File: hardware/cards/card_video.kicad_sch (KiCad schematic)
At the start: 30 parts, among them J1 HDMI_A, J2 VGA HD15, M1 Core2350B (8MB PSRAM), U2 74LVC245A, U3 74LVC245A, U4 74LVC245A, U5 74LVC245A, U6 74LVC245A, U7 74LVC245A

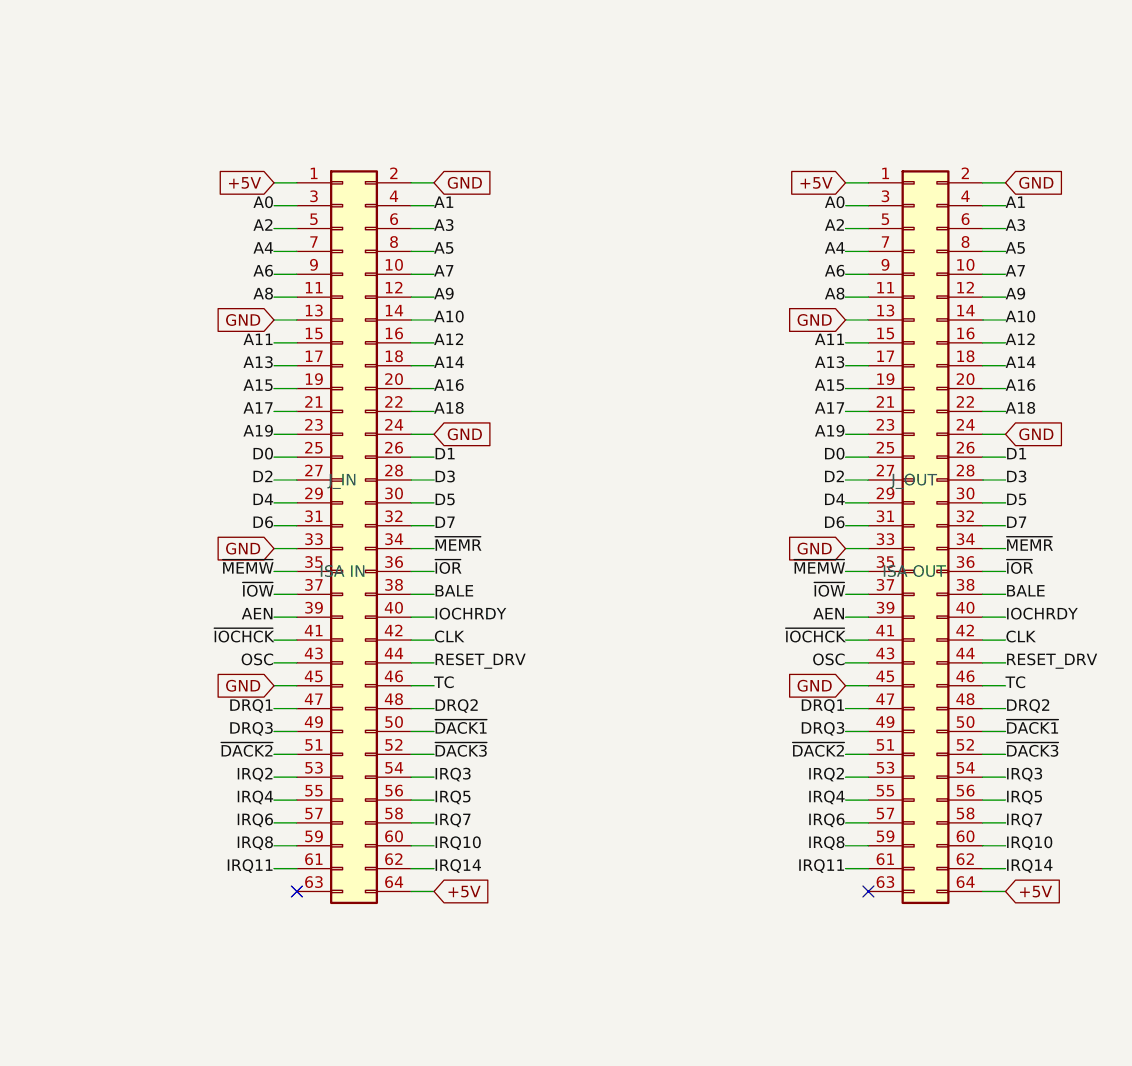
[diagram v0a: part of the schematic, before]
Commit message: Re-base ISA connector on standard 8-bit ISA pinout (60-pin, PicoGUS-style)
isa_conn now uses the standard 8-bit ISA edge pinout on a 60-pin 2.54mm header
(Conn_02x30_Odd_Even), matching the PicoGUS Bus_ISA_8bit layout so the sidecar and
dev cards are pin-compatible with real ISA cards (and 60-pin ribbon is easy to
source). The unused ISA analog rails are reclaimed: pin7 -5V->~{IOCHCK}, pin11
-12V->GND (extra return), pin15 +12V->IRQ8; pin13 reserved/0WS# left NC. Drops the
non-standard IRQ10/11/14 (16-bit-extension signals on a real AT); DACK0/REFRESH#
now on its standard pin (undriven, for card compatibility). Change is confined to
isa_conn.py; sidecar + all card_* sheets inherit it. Verified pin map and
connectivity (IOCHCK->Bus MCU, IRQ8->collector+RTC); zero structural ERC on
motherboard and all five cards.

Co-Authored-By: Claude Opus 4.8 (1M context) <noreply@anthropic.com>
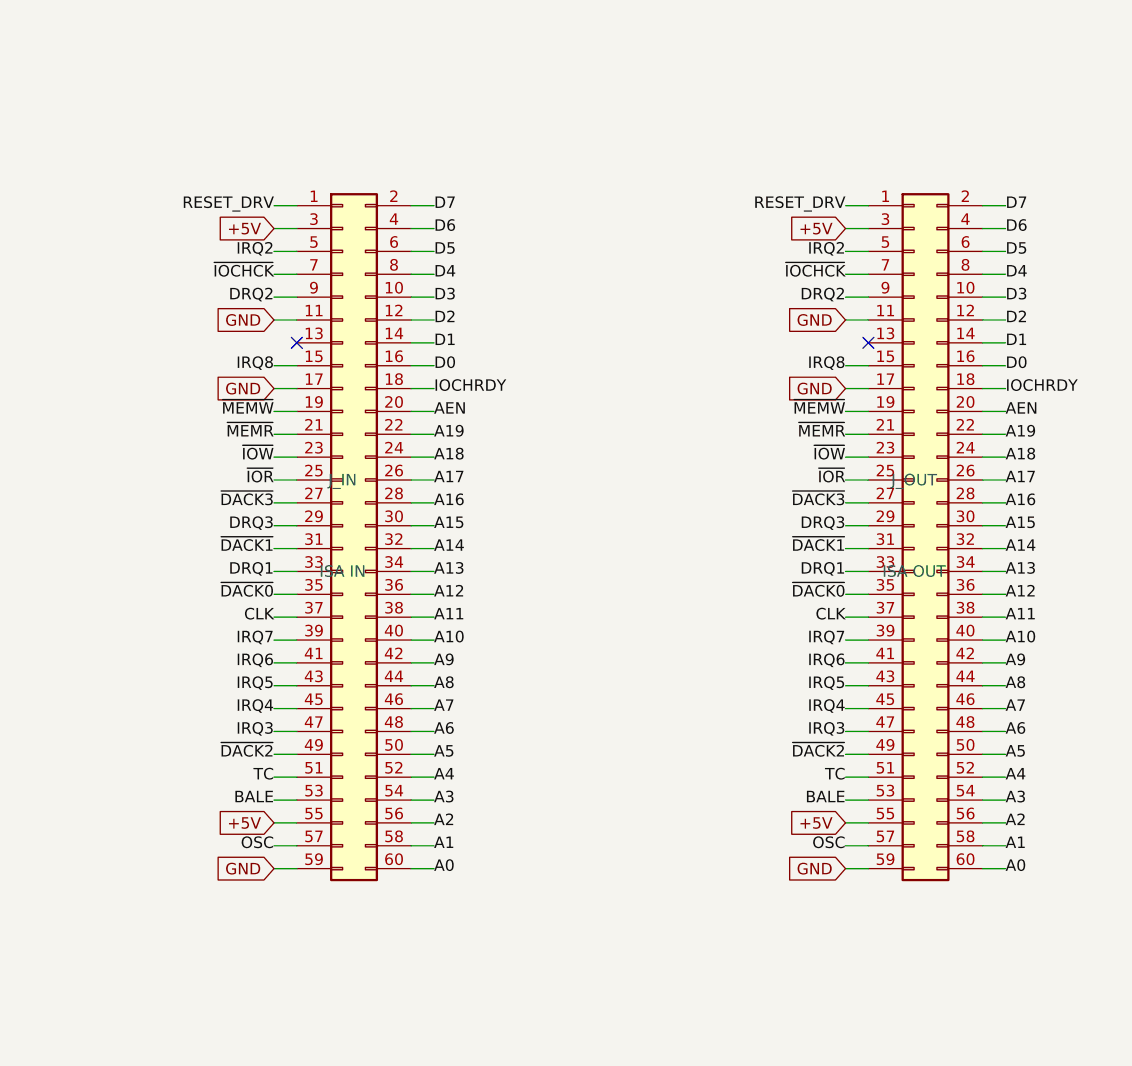
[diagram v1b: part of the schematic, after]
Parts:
- removed J_IN: ISA IN, symbol Connector_Generic:Conn_02x32_Odd_Even
- removed J_OUT: ISA OUT, symbol Connector_Generic:Conn_02x32_Odd_Even
- added J_IN: ISA IN, symbol Connector_Generic:Conn_02x30_Odd_Even
- added J_OUT: ISA OUT, symbol Connector_Generic:Conn_02x30_Odd_Even
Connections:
- net +5V: now also J_IN.3 (Pin_3), J_IN.55 (Pin_55), J_OUT.3 (Pin_3), J_OUT.55 (Pin_55)
- net A0: now also J_IN.60 (Pin_60), J_OUT.60 (Pin_60)
- net A1: now also J_IN.58 (Pin_58), J_OUT.58 (Pin_58)
- net A10: now also J_IN.40 (Pin_40), J_OUT.40 (Pin_40)
- net A11: now also J_IN.38 (Pin_38), J_OUT.38 (Pin_38)
- net A12: now also J_IN.36 (Pin_36), J_OUT.36 (Pin_36)
- net A13: now also J_IN.34 (Pin_34), J_OUT.34 (Pin_34)
- net A14: now also J_IN.32 (Pin_32), J_OUT.32 (Pin_32)
- net A15: now also J_IN.30 (Pin_30), J_OUT.30 (Pin_30)
- net A16: now also J_IN.28 (Pin_28), J_OUT.28 (Pin_28)
- net A17: now also J_IN.26 (Pin_26), J_OUT.26 (Pin_26)
- net A18: now also J_IN.24 (Pin_24), J_OUT.24 (Pin_24)
- net A19: now also J_IN.22 (Pin_22), J_OUT.22 (Pin_22)
- net A2: now also J_IN.56 (Pin_56), J_OUT.56 (Pin_56)
- net A3: now also J_IN.54 (Pin_54), J_OUT.54 (Pin_54)
- net A4: now also J_IN.52 (Pin_52), J_OUT.52 (Pin_52)
- net A5: now also J_IN.50 (Pin_50), J_OUT.50 (Pin_50)
- net A6: now also J_IN.48 (Pin_48), J_OUT.48 (Pin_48)
- net A7: now also J_IN.46 (Pin_46), J_OUT.46 (Pin_46)
- net A8: now also J_IN.44 (Pin_44), J_OUT.44 (Pin_44)
- net A9: now also J_IN.42 (Pin_42), J_OUT.42 (Pin_42)
- net AEN: now also J_IN.20 (Pin_20), J_OUT.20 (Pin_20)
- net BALE: now also J_IN.53 (Pin_53), J_OUT.53 (Pin_53)
- net CLK: now also J_IN.37 (Pin_37), J_OUT.37 (Pin_37)
- net D0: now also J_IN.16 (Pin_16), J_OUT.16 (Pin_16)
- net D1: now also J_IN.14 (Pin_14), J_OUT.14 (Pin_14)
- net D2: now also J_IN.12 (Pin_12), J_OUT.12 (Pin_12)
- net D3: now also J_IN.10 (Pin_10), J_OUT.10 (Pin_10)
- net D4: now also J_IN.8 (Pin_8), J_OUT.8 (Pin_8)
- net D5: now also J_IN.6 (Pin_6), J_OUT.6 (Pin_6)
- net D6: now also J_IN.4 (Pin_4), J_OUT.4 (Pin_4)
- net D7: now also J_IN.2 (Pin_2), J_OUT.2 (Pin_2)
- net DRQ1: now also J_IN.33 (Pin_33), J_OUT.33 (Pin_33)
- net DRQ2: now also J_IN.9 (Pin_9), J_OUT.9 (Pin_9)
- net DRQ3: now also J_IN.29 (Pin_29), J_OUT.29 (Pin_29)
- net GND: now also J_IN.11 (Pin_11), J_IN.17 (Pin_17), J_IN.59 (Pin_59), J_OUT.11 (Pin_11), J_OUT.17 (Pin_17), J_OUT.59 (Pin_59)
- net IOCHRDY: now also J_IN.18 (Pin_18), J_OUT.18 (Pin_18)
- net IRQ2: now also J_IN.5 (Pin_5), J_OUT.5 (Pin_5)
- net IRQ3: now also J_IN.47 (Pin_47), J_OUT.47 (Pin_47)
- net IRQ4: now also J_IN.45 (Pin_45), J_OUT.45 (Pin_45)
- net IRQ5: now also J_IN.43 (Pin_43), J_OUT.43 (Pin_43)
- net IRQ6: now also J_IN.41 (Pin_41), J_OUT.41 (Pin_41)
- net IRQ7: now also J_IN.39 (Pin_39), J_OUT.39 (Pin_39)
- net IRQ8: now also J_IN.15 (Pin_15), J_OUT.15 (Pin_15)
- net OSC: now also J_IN.57 (Pin_57), J_OUT.57 (Pin_57)
- net RESET_DRV: now also J_IN.1 (Pin_1), J_OUT.1 (Pin_1)
- net TC: now also J_IN.51 (Pin_51), J_OUT.51 (Pin_51)
- net ~{DACK1}: now also J_IN.31 (Pin_31), J_OUT.31 (Pin_31)
- net ~{DACK2}: now also J_IN.49 (Pin_49), J_OUT.49 (Pin_49)
- net ~{DACK3}: now also J_IN.27 (Pin_27), J_OUT.27 (Pin_27)
- net ~{IOCHCK}: now also J_IN.7 (Pin_7), J_OUT.7 (Pin_7)
- net ~{IOR}: now also J_IN.25 (Pin_25), J_OUT.25 (Pin_25)
- net ~{IOW}: now also J_IN.23 (Pin_23), J_OUT.23 (Pin_23)
- net ~{MEMR}: now also J_IN.21 (Pin_21), J_OUT.21 (Pin_21)
- net ~{MEMW}: now also J_IN.19 (Pin_19), J_OUT.19 (Pin_19)
- new net ~{DACK0}: J_IN.35 (Pin_35), J_OUT.35 (Pin_35)

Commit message: Drive ISA REFRESH# from the Bus MCU for DRAM-based cards
Pin 35 (DACK0/REFRESH#) net renamed ~{DACK0} -> ~{REFRESH} in isa_conn and is now
an active Bus MCU output (GPIO47, reclaimed from the redundant raw-~WR sense -- the
MCU tracks writes via the gated MEMW/IOW). Driven from the internal ~15us refresh
timer (same source as the 0x61-bit-4 toggle); a refresh cycle reuses the bus-master
engine to walk the row address on A0-A7 + pulse MEMR#, so DRAM ISA cards see a
standard refresh. ~{REFRESH} added to the Bus MCU interface. Verified it ties
sidecar<->Bus MCU and passes through J_IN<->J_OUT on every dev card; zero
structural ERC on motherboard and all five cards.

Co-Authored-By: Claude Opus 4.8 (1M context) <noreply@anthropic.com>
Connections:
- net ~{DACK0} renamed ~{REFRESH}
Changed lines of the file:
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@@
 		)
 	)
-	(label "~{DACK0}"
+	(label "~{REFRESH}"
 		(at 436.88 160.02 180)
 		(effects
@@
 		)
 	)
-	(label "~{DACK0}"
+	(label "~{REFRESH}"
 		(at 500.38 160.02 180)
 		(effects
@@
 		(instances
 			(project "card_video"
-				(path "/374d94a5-2c53-4835-9847-49239f55f3cf"
+				(path "/0c25f20b-85af-4bd6-a748-56afc32eeb49"
 					(reference "J_IN")
 					(unit 1)
@@
 		(instances
 			(project "card_video"
-				(path "/374d94a5-2c53-4835-9847-49239f55f3cf"
+				(path "/0c25f20b-85af-4bd6-a748-56afc32eeb49"
 					(reference "J_OUT")
 					(unit 1)
@@
 		(instances
 			(project "card_video"
-				(path "/374d94a5-2c53-4835-9847-49239f55f3cf"
+				(path "/0c25f20b-85af-4bd6-a748-56afc32eeb49"
 					(reference "M1")
 					(unit 1)
@@
 		(instances
 			(project "card_video"
-				(path "/374d94a5-2c53-4835-9847-49239f55f3cf"
+				(path "/0c25f20b-85af-4bd6-a748-56afc32eeb49"
 					(reference "C1")
 					(unit 1)
@@
 		(instances
 			(project "card_video"
-				(path "/374d94a5-2c53-4835-9847-49239f55f3cf"
+				(path "/0c25f20b-85af-4bd6-a748-56afc32eeb49"
 					(reference "C2")
 					(unit 1)
@@
 		(instances
 			(project "card_video"
-				(path "/374d94a5-2c53-4835-9847-49239f55f3cf"
+				(path "/0c25f20b-85af-4bd6-a748-56afc32eeb49"
 					(reference "C3")
 					(unit 1)
@@
 		(instances
 			(project "card_video"
-				(path "/374d94a5-2c53-4835-9847-49239f55f3cf"
+				(path "/0c25f20b-85af-4bd6-a748-56afc32eeb49"
 					(reference "U2")
 					(unit 1)
@@
 		(instances
 			(project "card_video"
-				(path "/374d94a5-2c53-4835-9847-49239f55f3cf"
+				(path "/0c25f20b-85af-4bd6-a748-56afc32eeb49"
 					(reference "U3")
 					(unit 1)
@@
 		(instances
 			(project "card_video"
-				(path "/374d94a5-2c53-4835-9847-49239f55f3cf"
+				(path "/0c25f20b-85af-4bd6-a748-56afc32eeb49"
 					(reference "U4")
 					(unit 1)
@@
 		(instances
 			(project "card_video"
-				(path "/374d94a5-2c53-4835-9847-49239f55f3cf"
+				(path "/0c25f20b-85af-4bd6-a748-56afc32eeb49"
 					(reference "U5")
 					(unit 1)
@@
 		(instances
 			(project "card_video"
-				(path "/374d94a5-2c53-4835-9847-49239f55f3cf"
+				(path "/0c25f20b-85af-4bd6-a748-56afc32eeb49"
 					(reference "U6")
 					(unit 1)
@@
 		(instances
 			(project "card_video"
-				(path "/374d94a5-2c53-4835-9847-49239f55f3cf"
+				(path "/0c25f20b-85af-4bd6-a748-56afc32eeb49"
 					(reference "U7")
 					(unit 1)
@@
 		(instances
 			(project "card_video"
-				(path "/374d94a5-2c53-4835-9847-49239f55f3cf"
+				(path "/0c25f20b-85af-4bd6-a748-56afc32eeb49"
 					(reference "J1")
 					(unit 1)
@@
 		(instances
 			(project "card_video"
-				(path "/374d94a5-2c53-4835-9847-49239f55f3cf"
+				(path "/0c25f20b-85af-4bd6-a748-56afc32eeb49"
 					(reference "R10")
 					(unit 1)
@@
 		(instances
 			(project "card_video"
-				(path "/374d94a5-2c53-4835-9847-49239f55f3cf"
+				(path "/0c25f20b-85af-4bd6-a748-56afc32eeb49"
 					(reference "R11")
 					(unit 1)
@@
 		(instances
 			(project "card_video"
-				(path "/374d94a5-2c53-4835-9847-49239f55f3cf"
+				(path "/0c25f20b-85af-4bd6-a748-56afc32eeb49"
 					(reference "R12")
 					(unit 1)
@@
 		(instances
 			(project "card_video"
-				(path "/374d94a5-2c53-4835-9847-49239f55f3cf"
+				(path "/0c25f20b-85af-4bd6-a748-56afc32eeb49"
 					(reference "R13")
 					(unit 1)
@@
 		(instances
 			(project "card_video"
-				(path "/374d94a5-2c53-4835-9847-49239f55f3cf"
+				(path "/0c25f20b-85af-4bd6-a748-56afc32eeb49"
 					(reference "R14")
 					(unit 1)
@@
 		(instances
 			(project "card_video"
-				(path "/374d94a5-2c53-4835-9847-49239f55f3cf"
+				(path "/0c25f20b-85af-4bd6-a748-56afc32eeb49"
 					(reference "R15")
 					(unit 1)
@@
 		(instances
 			(project "card_video"
-				(path "/374d94a5-2c53-4835-9847-49239f55f3cf"
+				(path "/0c25f20b-85af-4bd6-a748-56afc32eeb49"
 					(reference "R16")
 					(unit 1)
@@
 		(instances
 			(project "card_video"
-				(path "/374d94a5-2c53-4835-9847-49239f55f3cf"
+				(path "/0c25f20b-85af-4bd6-a748-56afc32eeb49"
 					(reference "R17")
 					(unit 1)
@@
 		(instances
 			(project "card_video"
-				(path "/374d94a5-2c53-4835-9847-49239f55f3cf"
+				(path "/0c25f20b-85af-4bd6-a748-56afc32eeb49"
 					(reference "R20")
 					(unit 1)
@@
 		(instances
 			(project "card_video"
-				(path "/374d94a5-2c53-4835-9847-49239f55f3cf"
+				(path "/0c25f20b-85af-4bd6-a748-56afc32eeb49"
 					(reference "R21")
 					(unit 1)
@@
 		(instances
 			(project "card_video"
-				(path "/374d94a5-2c53-4835-9847-49239f55f3cf"
+				(path "/0c25f20b-85af-4bd6-a748-56afc32eeb49"
 					(reference "R22")
 					(unit 1)
@@
 		(instances
 			(project "card_video"
-				(path "/374d94a5-2c53-4835-9847-49239f55f3cf"
+				(path "/0c25f20b-85af-4bd6-a748-56afc32eeb49"
 					(reference "R23")
 					(unit 1)
@@
 		(instances
 			(project "card_video"
-				(path "/374d94a5-2c53-4835-9847-49239f55f3cf"
+				(path "/0c25f20b-85af-4bd6-a748-56afc32eeb49"
 					(reference "R24")
 					(unit 1)
@@
 		(instances
 			(project "card_video"
-				(path "/374d94a5-2c53-4835-9847-49239f55f3cf"
+				(path "/0c25f20b-85af-4bd6-a748-56afc32eeb49"
 					(reference "R25")
 					(unit 1)
@@
 		(instances
 			(project "card_video"
-				(path "/374d94a5-2c53-4835-9847-49239f55f3cf"
+				(path "/0c25f20b-85af-4bd6-a748-56afc32eeb49"
 					(reference "R26")
 					(unit 1)
@@
 		(instances
 			(project "card_video"
-				(path "/374d94a5-2c53-4835-9847-49239f55f3cf"
+				(path "/0c25f20b-85af-4bd6-a748-56afc32eeb49"
 					(reference "R27")
 					(unit 1)
@@
 		(instances
 			(project "card_video"
-				(path "/374d94a5-2c53-4835-9847-49239f55f3cf"
+				(path "/0c25f20b-85af-4bd6-a748-56afc32eeb49"
 					(reference "J2")
 					(unit 1)

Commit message: JLCPCB sourcing pass: verify pinouts, LCSC part numbers, SMD build
Custom-symbol verification (open-questions Q5 resolved):
- MAX3241 symbol was wrong on nearly every pin and used MAX3243-style
  control names; regenerated to the real SSOP-28 pinout (SHDN#/EN#/
  R1OUTB/R2OUTB) and com_port rewired -- EN# must be GROUNDED (the old
  ~FORCEON-high would have disabled the receivers on real silicon)
- DS12C887 symbol wrong on 4 pins (DS=17, RESET#=18, IRQ#=19, SQW=23)

Sourcing (every part checked against the JLC DB; ~45 line items):
- New tools/parts.py maps (lib_id, value) -> LCSC; build.py applies it as
  an 'LCSC Part Num' property on every component (384 across the project)
- Sheets stay generic; stock-forced substitutions bound in the map:
  '374->'574 (parallel rewired), '163->'161, '157->HC157 (+HCT-buffered
  3.3V selects, I0/I1 swapped), '02->HC02, TCM809->MCP809, 2N3904->MMBT3904
- bus_mcu address counters moved to the 3.3V domain (HC161 on 3V3_BUS,
  loaded from MCU-side MD0-7; HCT244s read the 3.3V outputs at TTL Vih)
- 14.318 XOs are 3.3V-only parts: powered from 3V3, squared up via spare
  HCT gates (cpu_core U13, card_isatest U19)
- COM baud reference is now a 1.8432MHz crystal on the 16C550's XIN/XOUT
  (3.3V-only oscillators vs a 5V-only soft card)
- Supervisor QSPI header replaced with a real W25Q128JVSIQ
- Socket policy (fab installs sockets): V20 DIP-40, SRAM DIP-32 (no 5V
  512Kx8 SRAM at JLC at all), DS12C887 DIP-24, female headers for modules

Docs: CLAUDE.md fabrication-constraints section (SMD, 100x100mm, generic-
symbols rule, voltage-domain rule); README + hardware/README fab notes;
notes/jlcpcb-sourcing.md (decisions, thin-stock flags, not-at-JLC list);
stale questions-sidecar.md collapsed to its supersession record.

Rebuilt motherboard + cards: structural ERC 0, byte-identical rebuilds.

Co-Authored-By: Claude Fable 5 <noreply@anthropic.com>
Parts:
- C1, C2: LCSC Part Num (none) -> C14663
- C3: LCSC Part Num (none) -> C15850
- J1: LCSC Part Num (none) -> C2858275
- J_IN, J_OUT: LCSC Part Num (none) -> C2333
- M1: LCSC Part Num (none) -> C2897411
- R10, R11, R12, R13, R14, R15, R16, R17: LCSC Part Num (none) -> C22966
- R20, R23: LCSC Part Num (none) -> C22975
- R21, R24, R26: LCSC Part Num (none) -> C21190
- R22, R25, R27: LCSC Part Num (none) -> C23193
- U2, U3, U4, U5, U6, U7: LCSC Part Num (none) -> C6082
